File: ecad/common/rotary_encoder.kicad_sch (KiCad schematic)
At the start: 7 parts, among them Q6 RE1C002UN, SW11 PEL12T, U6 TLC5973

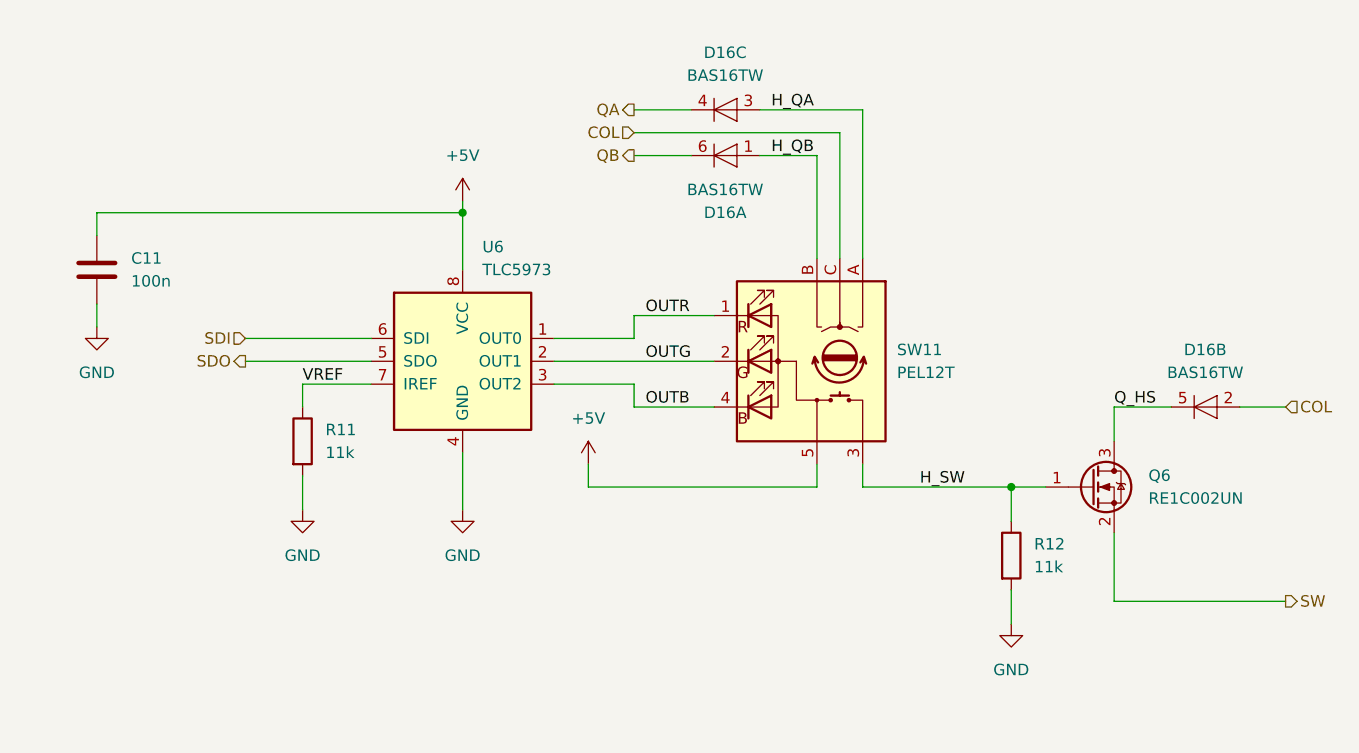
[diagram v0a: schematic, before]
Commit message: Uses WS2811 led communication everywhere
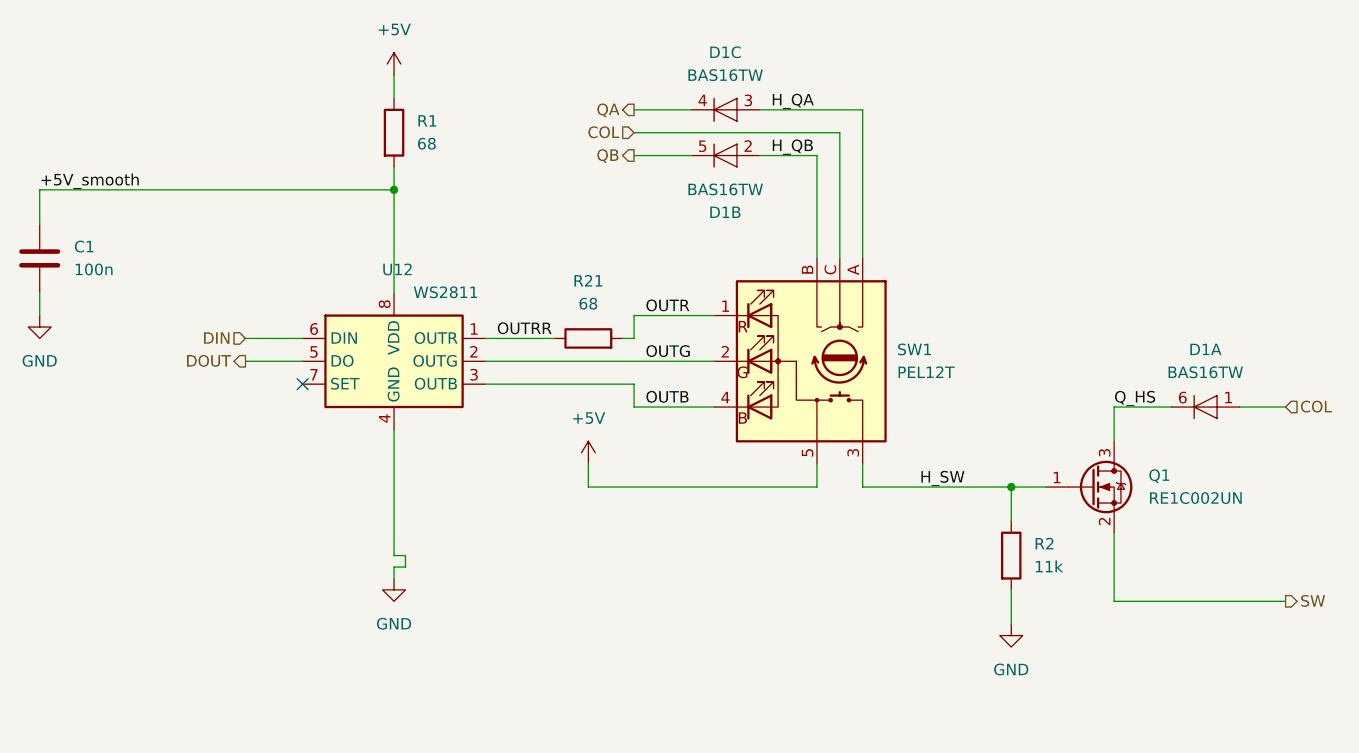
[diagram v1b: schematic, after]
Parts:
- removed U6: TLC5973, Package_SO:SOIC-8_3.9x4.9mm_P1.27mm, symbol Driver_LED:TLC5973
- added R21: 68, Resistor_SMD:R_0603_1608Metric, symbol Device:R
- added U12: WS2811, Package_SO:SOIC-8_3.9x4.9mm_P1.27mm, symbol Driver_LED:WS2811
- R1: renamed from R11; value 11k -> 68
- SW1: renamed from SW11; MPN (none) -> PEL12T-4225S-S1024
- renumbered C11 to C1, D16 to D1, Q6 to Q1, R12 to R2
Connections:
- net VREF is gone; now on net +5V: R1.1
- net +5V: no longer C1.1
- net COL: now also D1.1 (A); no longer D1.2 (A)
- net GND: now also U12.4 (GND); no longer R1.2
- net H_QB: now also D1.2 (A); no longer D1.1 (A)
- net OUTB: now also U12.3 (OUTB)
- net OUTG: now also U12.2 (OUTG)
- net OUTR: now also R21.2
- net QB: now also D1.5 (K); no longer D1.6 (K)
- net Q_HS: now also D1.6 (K); no longer D1.5 (K)
- new net +5V_smooth: C1.1, R1.2, U12.8 (VDD)
- new net DIN: U12.6 (DIN)
- new net DOUT: U12.5 (DO)
- new net OUTRR: R21.1, U12.1 (OUTR)
- no-connect marks 0 -> 1
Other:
- moved on the sheet: C1, D1A, D1B, R1

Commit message: WIP LED
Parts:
- removed C1: 100n, Capacitor_SMD:C_0603_1608Metric, symbol Device:C
- removed unit 1 of D1
- removed Q1: RE1C002UN, Package_TO_SOT_SMD:SOT-416, symbol Device:Q_NMOS_GSD
- removed R1, R21: 68, Resistor_SMD:R_0603_1608Metric, symbol Device:R
- removed R2: 11k, Resistor_SMD:R_0603_1608Metric, symbol Device:R
- removed U12: WS2811, Package_SO:SOIC-8_3.9x4.9mm_P1.27mm, symbol Driver_LED:WS2811
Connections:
- net +5V renamed LEDA
- net H_SW: no longer names the net of SW1.3
- net OUTB renamed LEDB
- net OUTG renamed LEDG
- net OUTR renamed LEDR

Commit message: [WIP] Layouting a matric led driver
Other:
- moved on the sheet: D1B, D1C, SW1

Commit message: Uses a LP5864 LED Matrix Driver for Top Section
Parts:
- D1: MPN (none) -> BAS16TW
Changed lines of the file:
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@@
+			)
+		)
+		(property "MPN" "BAS16TW"
+			(at 100.33 43.18 0)
+			(effects
+				(font
+					(size 1.27 1.27)
+				)
+				(hide yes)
+			)
+		)
+		(property "Manufacturer" ""
+			(at 100.33 43.18 0)
+			(effects
+				(font
+					(size 1.27 1.27)
+				)
+				(hide yes)
 			)
 		)
@@
 			)
 		)
+		(property "Manufacturer" ""
+			(at 113.03 71.12 90)
+			(effects
+				(font
+					(size 1.27 1.27)
+				)
+				(hide yes)
+			)
+		)
 		(pin "5"
 		)
@@
 			(at 100.33 48.26 0)
 			(effects
+				(font
+					(size 1.27 1.27)
+				)
+				(hide yes)
+			)
+		)
+		(property "MPN" "BAS16TW"
+			(at 100.33 48.26 0)
+			(effects
+				(font
+					(size 1.27 1.27)
+				)
+				(hide yes)
+			)
+		)
+		(property "Manufacturer" ""
+			(at 100.33 48.26 0)
+			(effects
